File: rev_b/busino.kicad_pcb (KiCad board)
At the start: 2 copper layers, 100 x 100 mm, 62 parts, among them J1 TERMINATE_JUMPER, J2 LED_JUMPER, SW1 2_LEAD_PUSH_BUTTON, U1 LM2940CT-5.0, U2 MCP2562, U3 LM1117T-3.3, U4 74x06, U5 ATMEGA324_DIP40, X1 16MHz, X2 OSHW_LOGO

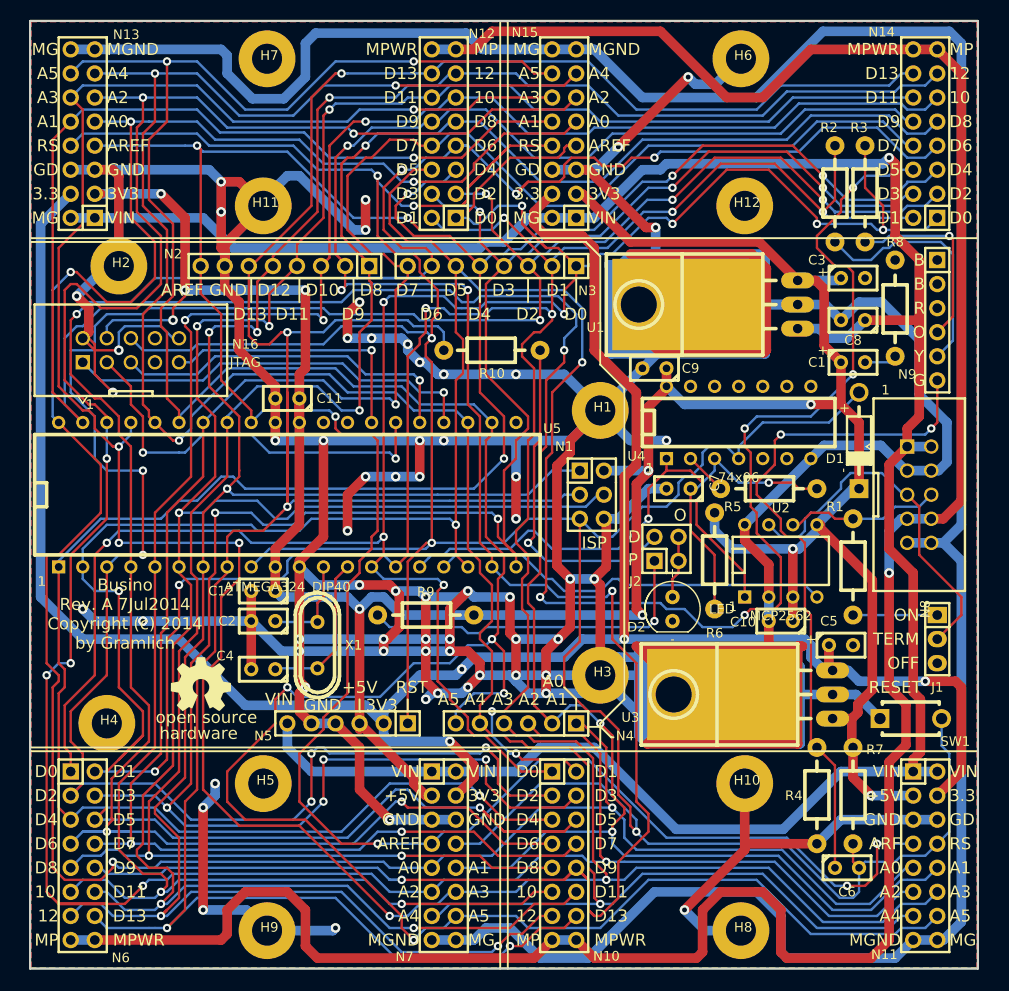
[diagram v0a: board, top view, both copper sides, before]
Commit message: Switched libraries to use Rev. B libraries.
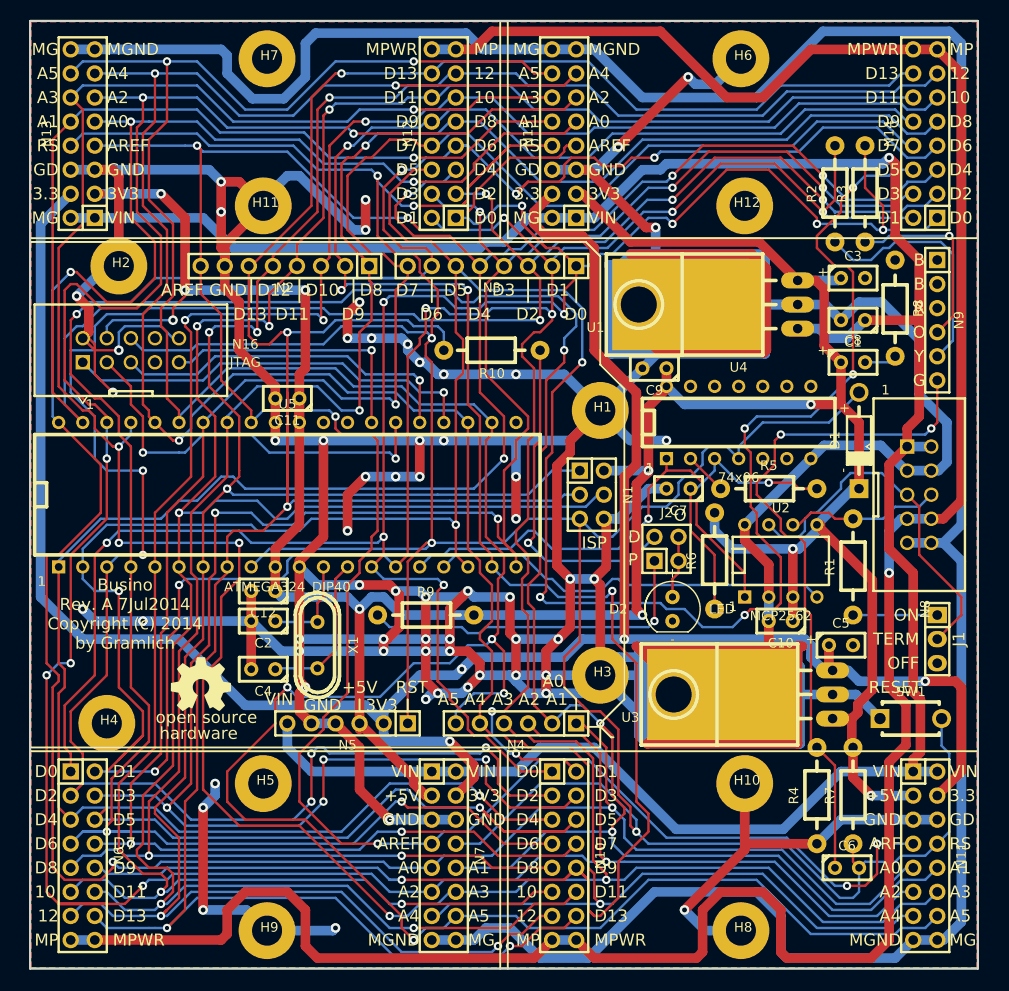
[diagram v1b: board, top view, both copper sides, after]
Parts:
- C1, C10, C11, C12, C2, C3, C4, C5, C6, C7, C8, C9: footprint Busino_Rev_A:Capacitor3MMDiscRM2.5 -> Busino_Rev_B:Capacitor3MMDiscRM2.5
- D1: footprint Busino_Rev_A:Diode_DO-41_SOD81_Horizontal_RM10 -> Busino_Rev_B:Diode_DO-41_SOD81_Horizontal_RM10
- D2: footprint Busino_Rev_A:T1_LED -> Busino_Rev_B:T1_LED
- H1, H10, H11, H12, H2, H3, H4, H5, H6, H7, H8, H9: footprint Busino_Rev_A:MountingHole_3mm -> Busino_Rev_B:MountingHole_3mm
- J1: footprint Busino_Rev_A:Pin_Header_Straight_1x03 -> Busino_Rev_B:Pin_Header_Straight_1x03
- J2: footprint Busino_Rev_A:Pin_Header_Straight_2x02 -> Busino_Rev_B:Pin_Header_Straight_2x02
- N1: footprint Busino_Rev_A:Pin_Header_Straight_2x03 -> Busino_Rev_B:Pin_Header_Straight_2x03
- N10, N11, N12, N13, N14, N15, N6, N7: footprint Busino_Rev_A:Pin_Header_Straight_2x08 -> Busino_Rev_B:Pin_Header_Straight_2x08
- N16, N8: footprint Busino_Rev_A:Pin_Header_Straight_2x05_Shrouded -> Busino_Rev_B:Pin_Header_Straight_2x05_Shrouded
- N2, N3: footprint Busino_Rev_A:Pin_Header_Straight_1x08 -> Busino_Rev_B:Pin_Header_Straight_1x08
- N4, N5, N9: footprint Busino_Rev_A:Pin_Header_Straight_1x06 -> Busino_Rev_B:Pin_Header_Straight_1x06
- R1, R10, R2, R3, R4, R5, R6, R7, R8, R9: footprint Busino_Rev_A:Resistor_Horizontal__400 -> Busino_Rev_B:Resistor_Horizontal__400
- SW1: footprint Busino_Rev_A:BUTTON_6.5MM -> Busino_Rev_B:BUTTON_6.5MM
- U1, U3: footprint Busino_Rev_A:Regulator_TO_220_Horizontal -> Busino_Rev_B:Regulator_TO_220_Horizontal
- U2: footprint Busino_Rev_A:DIP-8__300 -> Busino_Rev_B:DIP-8__300
- U4: footprint Busino_Rev_A:DIP-14__300 -> Busino_Rev_B:DIP-14__300
- U5: footprint Busino_Rev_A:DIP-40__600 -> Busino_Rev_B:DIP-40__600
- X1: footprint Busino_Rev_A:Crystal_HC49-U_Vertical -> Busino_Rev_B:Crystal_HC49-U_Vertical
- X2: footprint Busino_Rev_A:OSHW_LOGO_250mil -> Busino_Rev_B:OSHW_LOGO_250mil
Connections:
- net +5V renamed VCC
- J1 pad 3: (no net) -> Net-(J1-Pad3)
- N16 pad 7: (no net) -> Net-(N16-Pad7)
- N16 pad 8: (no net) -> Net-(N16-Pad8)
- N9 pad 2: (no net) -> Net-(N9-Pad2)
- N9 pad 3: (no net) -> Net-(N9-Pad3)
- U5 pad 21: (no net) -> Net-(U5-Pad21)
- U5 pad 28: (no net) -> Net-(U5-Pad28)
- U5 pad 29: (no net) -> Net-(U5-Pad29)

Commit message: Add in some derived files.
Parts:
- D1: value SCHOTTKY_DIODE_VERT -> SD101C-TR
- R10, R9: value R_VERT -> 470
- U3: value LM1117T-3.3 -> LM1117
- turned C5 to 180 degrees
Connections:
- U3 pad 1: VCC -> GND
- U3 pad 2: GND -> +3.3V
- U3 pad 3: +3.3V -> VCC
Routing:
- net GND: track 943.1 -> 816.6 mm
- net VCC: track 320.5 -> 324.5 mm
- net +3.3V: track 241.1 -> 243.1 mm

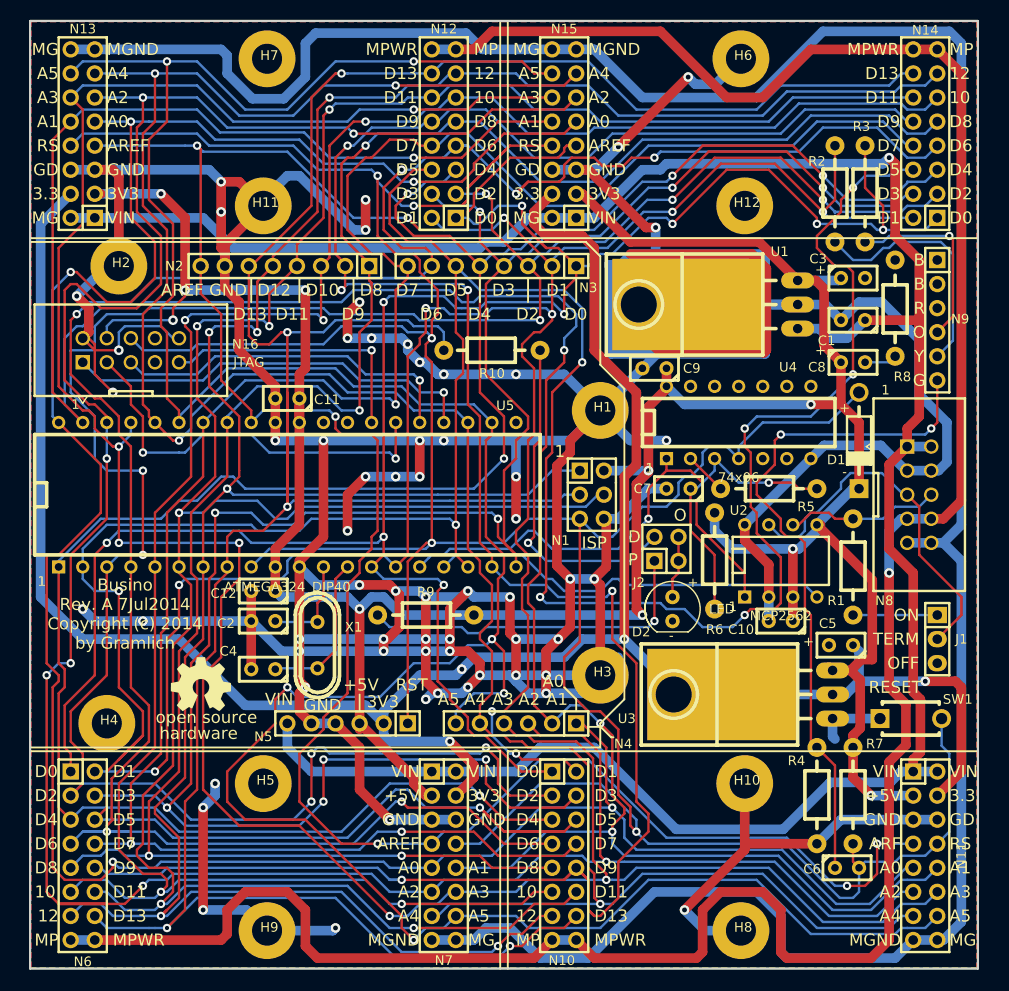
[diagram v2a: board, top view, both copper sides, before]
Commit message: Improved schematic description.  Added missiong wire from processor pin 21 to pin 6.
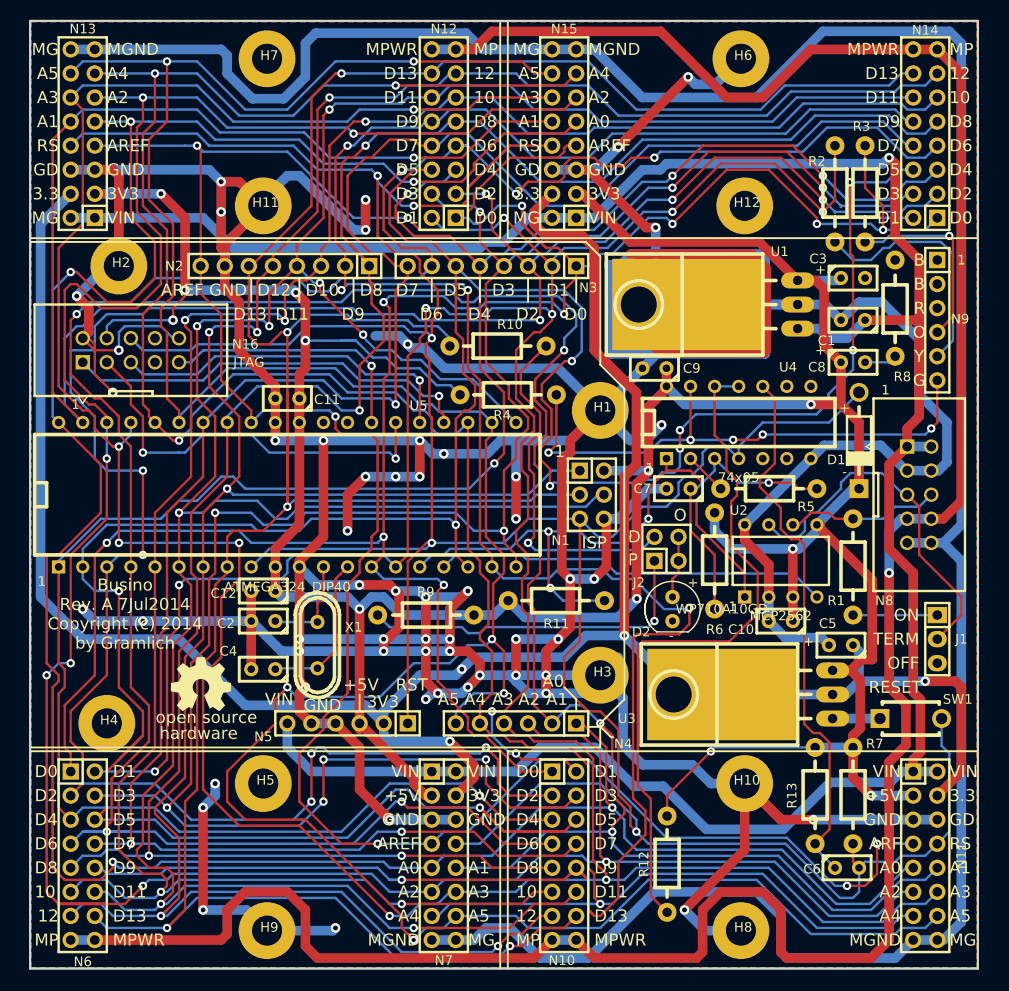
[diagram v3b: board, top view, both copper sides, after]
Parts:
- added R11: 100K, Busino_Rev_B:Resistor_Horizontal__400, F.Cu at (81.7, 87.4)
- added R12: 100K, Busino_Rev_B:Resistor_Horizontal__400, F.Cu at (93.4, 115.2)
- added R13: 10K, Busino_Rev_B:Resistor_Horizontal__400, F.Cu at (109.0, 108.0)
- D2: value LED -> WP710A10GD
- R4: value 1K -> 100K
- SW1: value 2_LEAD_PUSH_BUTTON -> MJTP1243
- U3: value LM1117 -> LM1117T-3.3
- U4: value 74x06 -> 74x05
- moved R4 53.4 mm to (76.6, 65.7), turned to 180 degrees
- moved R10 0.78 mm to (75.6, 60.5)
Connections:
- N9 pad 6: Net-(C6-Pad1) -> Net-(N9-Pad6)
- R4 pad 1: GND -> Net-(N9-Pad6)
- R4 pad 2: Net-(C6-Pad1) -> VCC
- U4 pad 10: (no net) -> Net-(C6-Pad1)
- U4 pad 11: (no net) -> Net-(R12-Pad1)
- U4 pad 12: (no net) -> Net-(R12-Pad1)
- U4 pad 13: (no net) -> Net-(N9-Pad6)
- U5 pad 21: Net-(U5-Pad21) -> /Arduino Shield/D11
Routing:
- net Net-(R12-Pad1): track 0.00 -> 72.3 mm
- net Net-(N9-Pad6): track 0.00 -> 58.9 mm, vias 0 -> 5
- net VCC: track 324.5 -> 367.6 mm, vias 10 -> 12
- net /Arduino Shield/D5: track 340.3 -> 306.4 mm
- net /Arduino Shield/D11: track 271.6 -> 302.2 mm, vias 6 -> 8
- net Net-(C6-Pad1): track 72.4 -> 57.4 mm, vias 2 -> 0
- net Net-(R11-Pad1): track 53.7 -> 65.5 mm, vias 1 -> 3
- net /Arduino Shield/D9: track 247.3 -> 258.1 mm
- net GND: track 816.6 -> 824.1 mm, vias 61 -> 55
- net /Arduino Shield/D6: track 253.4 -> 246.3 mm
- net /Arduino Shield/D3: track 230.6 -> 227.2 mm
- net Net-(J2-Pad2): track 36.0 -> 37.9 mm
- net /Arduino Shield/D10: track 225.7 -> 223.9 mm
- net /Arduino Shield/A1: track 280.6 -> 282.0 mm
- net /Arduino Shield/A4: track 252.3 -> 253.7 mm
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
